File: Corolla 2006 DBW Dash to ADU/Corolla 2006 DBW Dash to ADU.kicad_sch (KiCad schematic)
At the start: 4 parts

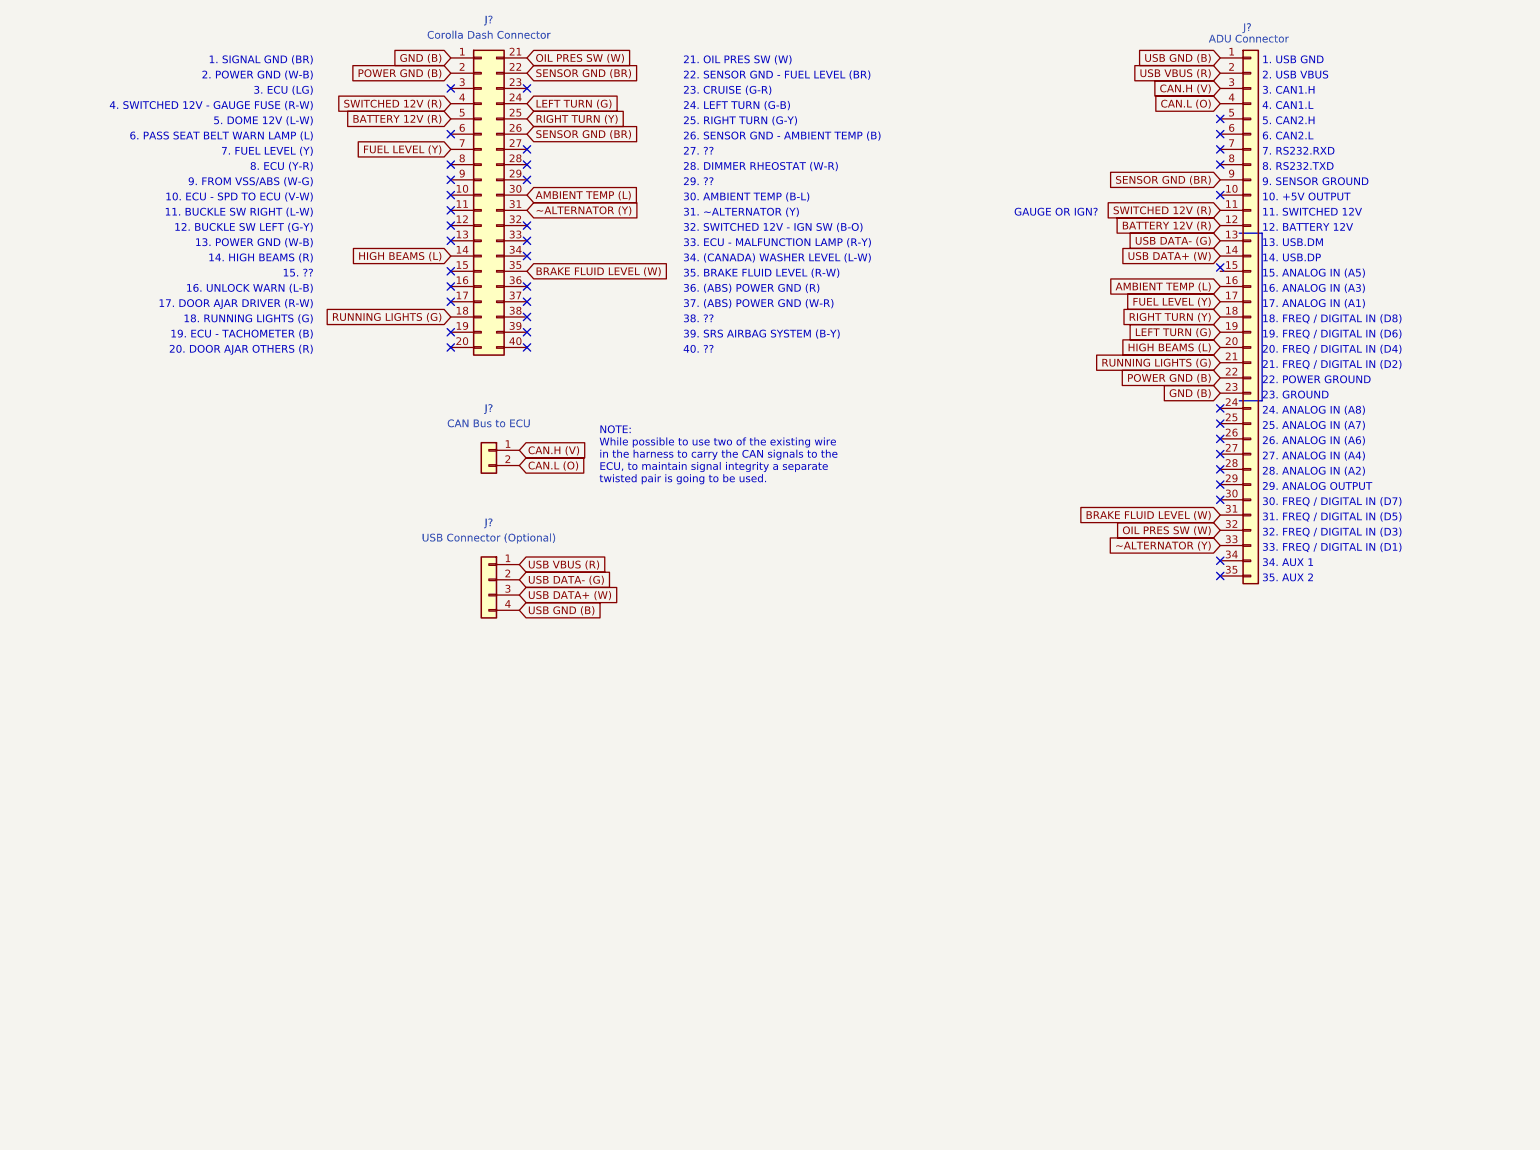
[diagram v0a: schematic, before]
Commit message: Added the rotary switch connector and fixed a few wires.
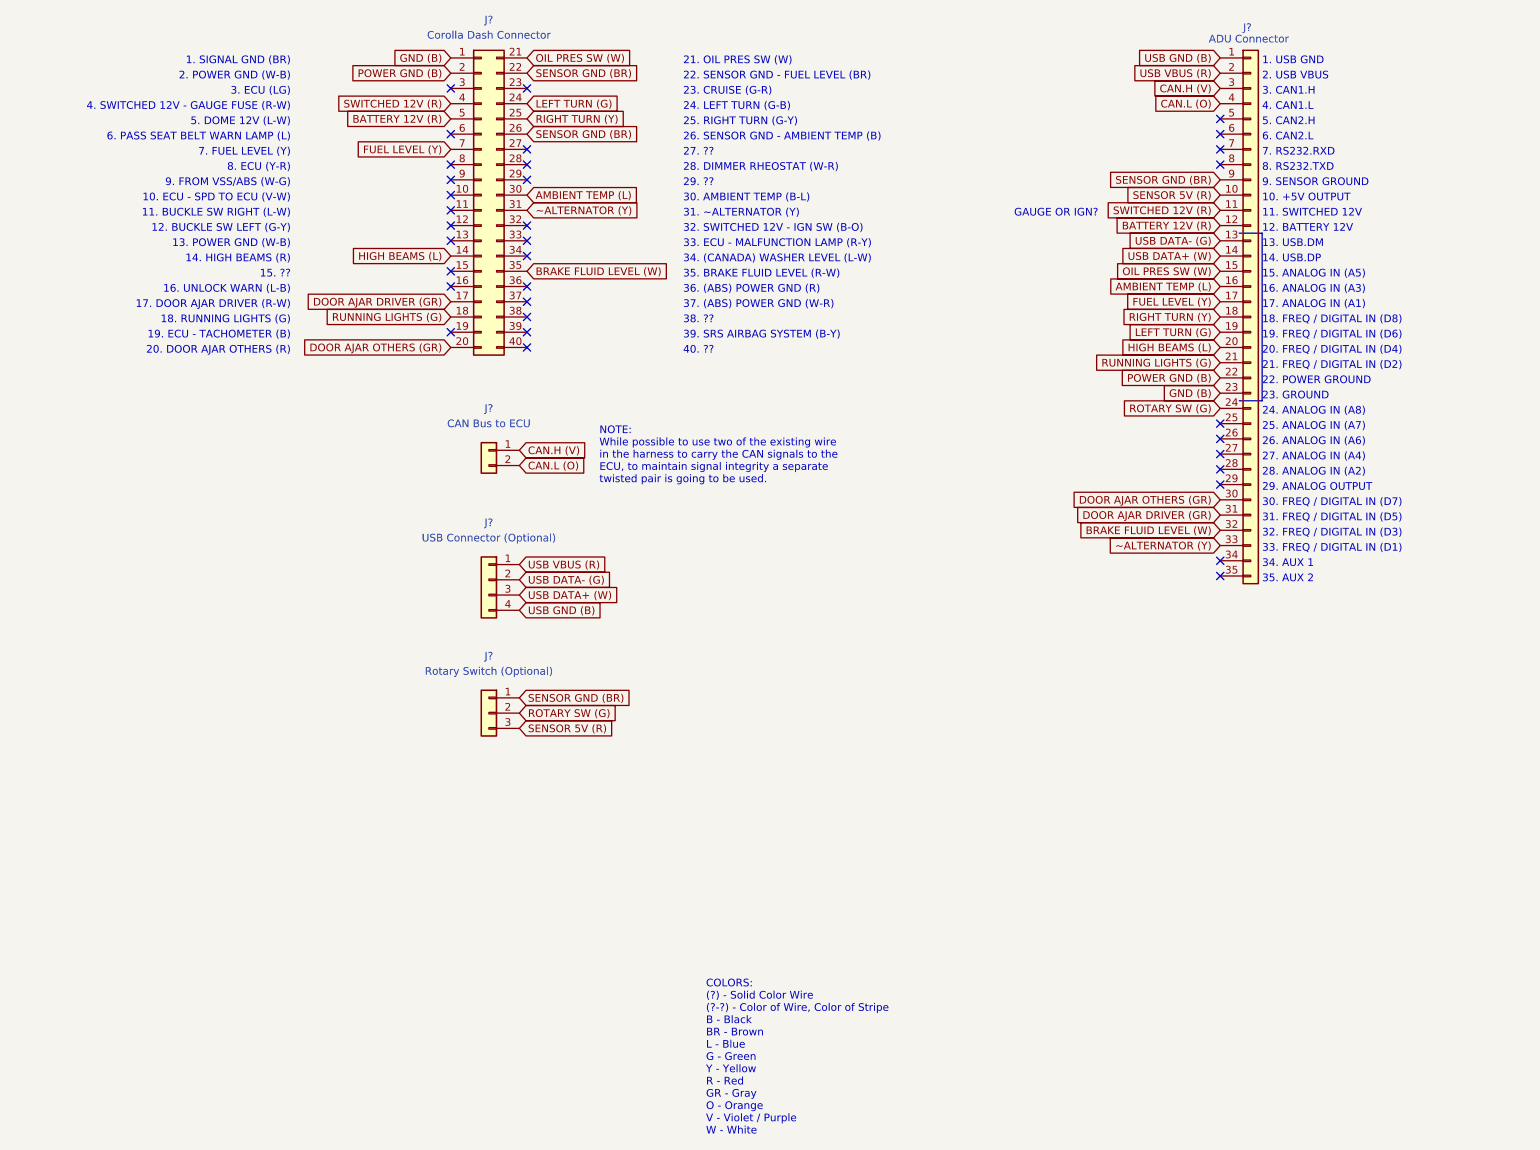
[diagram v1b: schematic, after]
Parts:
- added J?: Rotary Switch (Optional), symbol Connector_Generic:Conn_01x03
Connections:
- net BRAKE FLUID LEVEL (W): now also J?.32 (Pin_32); no longer J?.31 (Pin_31)
- net OIL PRES SW (W): now also J?.15 (Pin_15); no longer J?.32 (Pin_32)
- net SENSOR GND (BR): now also J?.1 (Pin_1)
- net SENSOR 5V (R): now reaches J?.10 (Pin_10)
- net SENSOR 5V (R): now also J?.3 (Pin_3)
- net ROTARY SW (G): now reaches J?.24 (Pin_24)
- net ROTARY SW (G): now also J?.2 (Pin_2)
- net DOOR AJAR OTHERS (GR): now reaches J?.30 (Pin_30)
- net DOOR AJAR OTHERS (GR): now also J?.20 (Pin_20)
- net DOOR AJAR DRIVER (GR): now reaches J?.17 (Pin_17)
- net DOOR AJAR DRIVER (GR): now also J?.31 (Pin_31)
- no-connect marks 40 -> 34
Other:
- note added: "COLORS: (?) - Solid Color Wire (?-?) - Color of Wire, Color of Stripe B - Black BR - Brown L - Blue G - Green Y - Yellow R - Red GR - Gray O - Orange V - Violet / Purple W - White"

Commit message: Adding updates and the 2006 DBW schematic.
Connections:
- net at J?.10 (Pin_10): now also J?.9 (Pin_9)
- no-connect marks 34 -> 32
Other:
- note added: "VSS to ECU Jumper"
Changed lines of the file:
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@@
     (comment 4 "Wired for ECU Masters EMU Black, not factory ECU")
   )
-  (no_connect (at 78.105 43.815))
   (no_connect (at 78.105 41.275))
   (no_connect (at 78.105 53.975))
   (no_connect (at 78.105 48.895))
-  (no_connect (at 78.105 46.355))
   (no_connect (at 78.105 51.435))
   (no_connect (at 78.105 61.595))
@@
   (no_connect (at 206.375 33.655))
   (no_connect (at 206.375 41.275))
+  (wire (pts (xy 76.2 46.355) (xy 78.105 46.355))
+    (stroke (width 0) (type default) (color 0 0 0 0))
+  )
   (polyline (pts (xy 209.55 52.705) (xy 213.36 52.705))
     (stroke (width 0) (type default) (color 0 0 0 0))
   )
+  (wire (pts (xy 76.2 43.815) (xy 76.2 46.355))
+    (stroke (width 0) (type default) (color 0 0 0 0))
+  )
   (polyline (pts (xy 209.55 80.645) (xy 213.36 80.645))
+    (stroke (width 0) (type default) (color 0 0 0 0))
+  )
+  (wire (pts (xy 78.105 43.815) (xy 76.2 43.815))
     (stroke (width 0) (type default) (color 0 0 0 0))
   )
@@
     (effects (font (size 1.27 1.27)) (justify right bottom))
   )
+  (text "VSS to ECU Jumper" (at 75.565 46.355 180)
+    (effects (font (size 1.27 1.27)) (justify right bottom))
+  )

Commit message: Now have a PCB to try.
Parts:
- removed J?: ADU Connector, symbol Connector_Generic:Conn_01x35
- added J5: Oil/Water Temp Sensor (Optional), Connector_Wire:SolderWire-0.75sqmm_1x02_P4.8mm_D1.25mm_OD2.3mm_Relief, symbol Connector_Generic:Conn_01x02
- added J6: CAN Bus Two (Optional), Connector_Wire:SolderWire-0.75sqmm_1x02_P4.8mm_D1.25mm_OD2.3mm_Relief, symbol Connector_Generic:Conn_01x02
- added J7: ADU_Connector, ecumaster:Wires for ADU Connector, symbol ecu_masters:ADU_Connector
- added JP1, JP2, JP4: SolderJumper_3_Open, Jumper:SolderJumper-3_P1.3mm_Open_RoundedPad1.0x1.5mm_NumberLabels, symbol Jumper:SolderJumper_3_Open
- added JP3: SolderJumper_2_Open, Jumper:SolderJumper-2_P1.3mm_Open_RoundedPad1.0x1.5mm, symbol Jumper:SolderJumper_2_Open
- J1: renamed from J?; footprint (none) -> toyota:2006 Corolla Dash Connector
- J2: renamed from J?; footprint (none) -> Connector_Wire:SolderWire-0.75sqmm_1x02_P4.8mm_D1.25mm_OD2.3mm_Relief
- J3: renamed from J?; footprint (none) -> Connector_Wire:SolderWire-0.25sqmm_1x04_P4.2mm_D0.65mm_OD1.7mm_Relief
- J4: renamed from J?; footprint (none) -> Connector_Wire:SolderWire-0.75sqmm_1x03_P4.8mm_D1.25mm_OD2.3mm_Relief
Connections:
- net AMBIENT TEMP (L): now also J7.16 (Analog_In_A3)
- net BATTERY 12V (R): now also J7.12 (Battery_12V)
- net BRAKE FLUID LEVEL (W): now also J7.27 (Analog_In_A4)
- net DOOR AJAR DRIVER (GR): now also J7.31 (Digital_In_D5)
- net DOOR AJAR OTHERS (GR): now also J7.30 (Digital_In_D7)
- net FUEL LEVEL (Y): now also J7.17 (Analog_In_A1)
- net GND (B): now also J7.23 (Ground)
- net HIGH BEAMS (L): now also J7.20 (Digital_In_D4)
- net LEFT TURN (G): now also J7.19 (Digital_In_D6)
- net OIL PRES SW (W): now also J7.15 (Analog_In_A5)
- net POWER GND (B): now also J7.22 (Power_Ground)
- net RIGHT TURN (Y): now also J7.18 (Digital_In_D8)
- net ROTARY SW (G): now also J7.24 (Analog_In_A8)
- net RUNNING LIGHTS (G): now also J7.21 (Digital_In_D2)
- net SENSOR 5V (R): now also J7.10 (+5V_Output)
- net SENSOR GND (BR): now also J5.1 (Pin_1), J7.9 (Sensor_Ground)
- net SWITCHED 12V (R): now also J7.11 (Switched_12V)
- net USB DATA+ (W): now also J7.14 (USB.DP)
- net USB DATA- (G): now also J7.13 (USB.DM)
- net USB GND (B): now also J7.1 (USB.GND)
- net USB VBUS (R): now also J7.2 (USB.VBUS)
- net ~ALTERNATOR (Y): now also J7.28 (Analog_In_A2)
- net SPEED SENDOR (W-G): now reaches J1.10 (Pin_10), J1.9 (Pin_9)
- net SPEED SENDOR (W-G): now also JP3.2 (B)
- net TACHOMETER (B): now reaches J1.19 (Pin_19)
- net TACHOMETER (B): now also JP1.2 (C)
- net MALFUNCTION LAMP (R-Y): now reaches J1.33 (Pin_33)
- net MALFUNCTION LAMP (R-Y): now also JP2.2 (C)
- net WATER TEMP (Y-R): now reaches J1.8 (Pin_8)
- net WATER TEMP (Y-R): now also JP4.1 (A)
- net CAN.H (V) renamed CAN1.H (V)
- net CAN1.H (V): now also J7.3 (CAN1.H), JP1.3 (B)
- net CAN.L (O) renamed CAN1.L (O)
- net CAN1.L (O): now also J7.4 (CAN1.L), JP2.3 (B)
- new net A6 - BAD LAMP: J7.26 (Analog_In_A6), JP2.1 (A)
- new net A7 - OIL/WATER TEMP: J7.25 (Analog_In_A7), JP4.2 (C)
- new net CAN2.H: J6.1 (Pin_1), J7.5 (CAN2.H)
- new net CAN2.L: J6.2 (Pin_2), J7.6 (CAN2.L)
- new net D1 - RPM: J7.33 (Digital_In_D1), JP1.1 (A)
- new net D3 - SPEED: J7.32 (Digital_In_D3), JP3.1 (A)
- new net OIL/WATER TEMP CONN: J5.2 (Pin_2), JP4.3 (B)
- no-connect marks 32 -> 23
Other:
- note added: "36. ABS OR POWER GND (R)"
- note added: "37. ABS OR POWER GND (W-R)"
- note added: "8. ECU - WATER TEMP (Y-R)"
- note added: "NOTE: Connect 1 & 2 for Factory ECU Leave Open for ECU Master Black"
- note added: "NOTE: Connect 1 & 2 for Factory ECU Leave Open for ECU Master Black Connect 2 & 3 to pass CAN through factory harness"
- note added: "NOTE: Connect 1 & 2 for Factory ECU Leave Open for ECU Master Black Connect 2 & 3 to use external temperature sensor"
- note added: "NOTE: This could also be used as a button input."
- note added: "NOTE: While possible to use two of the existing wire in the harness to carry the CAN signals to the ECU, to maintain signal integrity a separate twisted pair can be used."
- note removed: "36. (ABS) POWER GND (R)"
- note removed: "37. (ABS) POWER GND (W-R)"
- note removed: "8. ECU (Y-R)"
- note removed: "GAUGE OR IGN?"
- note removed: "NOTE: While possible to use two of the existing wire in the harness to carry the CAN signals to the ECU, to maintain signal integrity a separate twisted pair is going to be used."
- company: DadBodCarMod, LLC -> DadBodCarMod LLC
- title: Corolla 2006 DBW Dash to ADU Adapter -> Corolla 9th Gen ADU Dash Connector
- moved on the sheet: J2, J3, J4
